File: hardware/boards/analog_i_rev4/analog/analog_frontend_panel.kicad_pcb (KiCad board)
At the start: 4 copper layers, 257 parts, among them IC1 INA826AIDR, IC10 INA826AIDR, IC1001 INA826AIDR, IC12 INA826AIDR, IC13 TLV333IDBVR, IC14 TLV333IDBVR, IC15 INA826AIDR, IC16 TLV333IDBVR, IC17 TLV333IDBVR, IC18 INA826AIDR, IC19 TLV333IDBVR, IC2 INA826AIDR, IC20 TLV333IDBVR, IC21 INA826AIDR, IC22 TLV333IDBVR, IC23 TLV333IDBVR, IC24 INA826AIDR, IC25 TLV333IDBVR, IC26 TLV333IDBVR, IC27 INA826AIDR, IC28 TLV333IDBVR, IC29 TLV333IDBVR, IC3 INA826AIDR, IC3001 INA826AIDR, IC3002 INA826AIDR, IC32001 BD42540FJ-CE2, IC33001 BD42540FJ-CE2, IC34001 BD42540FJ-CE2, IC35001 BD42540FJ-CE2, IC36001 BD42540FJ-CE2, IC4 INA826AIDR, IC5 INA826AIDR, IC6 INA826AIDR, IC7 INA826AIDR, IC8 INA826AIDR, J10 Screw_Terminal_01x03, J1001 Screw_Terminal_01x04, J11 Screw_Terminal_01x03, J12 AM-K-PCB, J13 AM-K-PCB, J14 AM-K-PCB, J15 AM-K-PCB, J16 Screw_Terminal_01x03, J17 Screw_Terminal_01x03, J18 Screw_Terminal_01x03, J19 Screw_Terminal_01x03, J20 Screw_Terminal_01x03, J22 Screw_Terminal_01x03, J3 Screw_Terminal_01x04, J3004 Screw_Terminal_01x04, J3005 Screw_Terminal_01x04, J4 Screw_Terminal_01x04, J5 Screw_Terminal_01x04, J8 Screw_Terminal_01x03, J9 Screw_Terminal_01x03, U1 NTJD4001NT1G, U1001 TLV3201AIDBVR, U1002 TLV3201AIDBVR, U1003 TLV3201AIDBVR, U1004 TLV3201AIDBVR, U1005 TLV3201AIDBVR, U2 NTJD4001NT1G, U3 NTJD4001NT1G, U4 NTJD4001NT1G, U5 NTJD4001NT1G, U6 NTJD4001NT1G

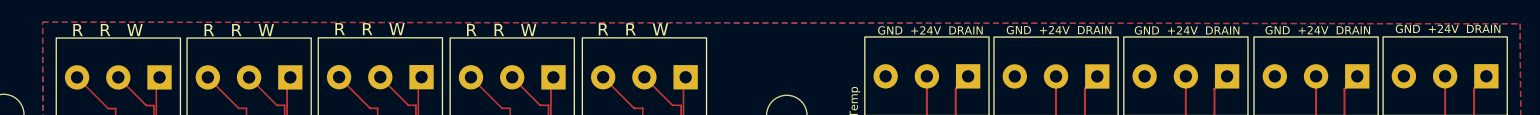
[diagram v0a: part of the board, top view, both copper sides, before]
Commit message: flip more silkscreen labels
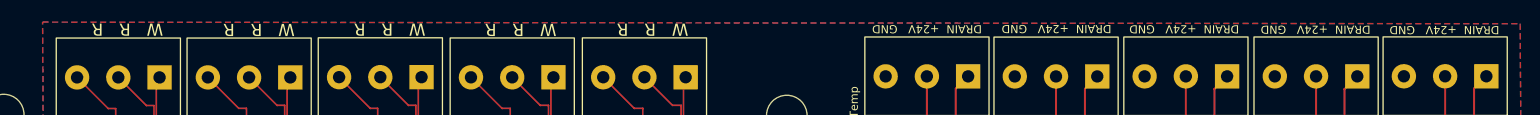
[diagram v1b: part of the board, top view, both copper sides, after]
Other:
- board text added: "DRAIN +24V GND"
- board text added: "W R R"
- board text removed: "GND +24V DRAIN"
- board text removed: "R R W"

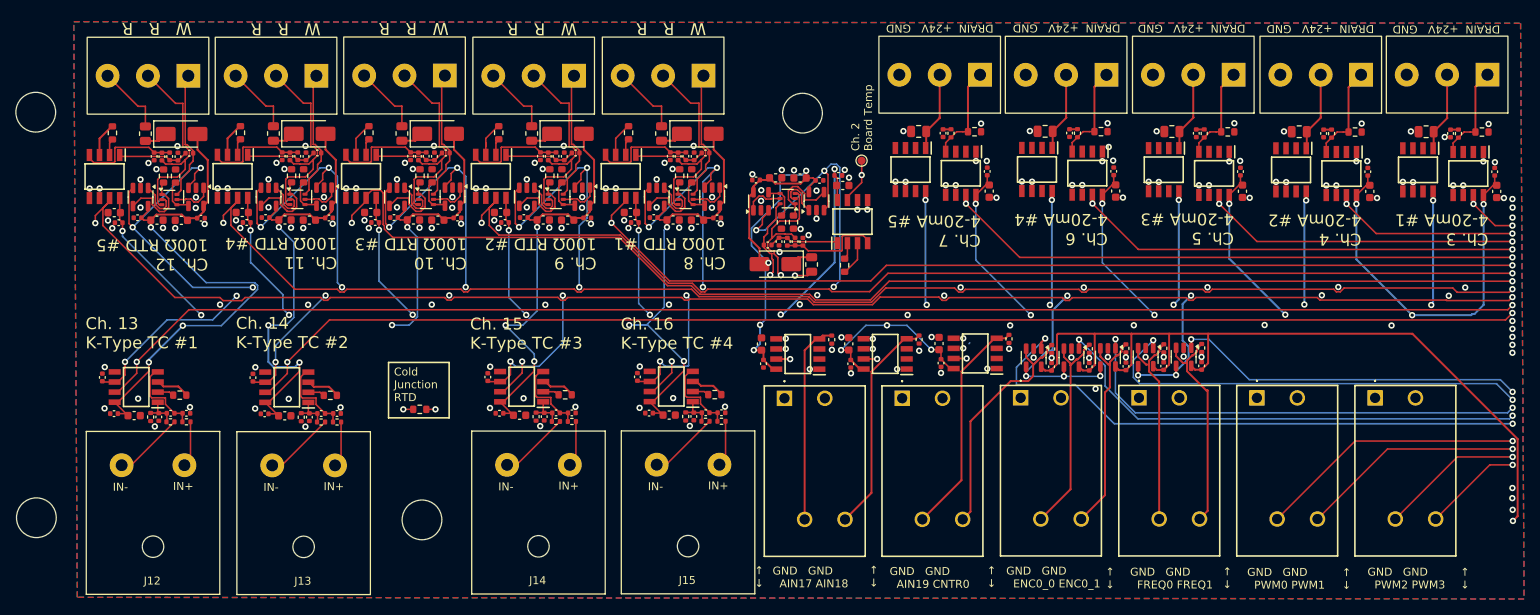
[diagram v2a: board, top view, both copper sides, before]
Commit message: Analog I Rev 4.0.2 (#17)
## 2025-02-22 Hardware - Analog I Rev 4.0.2

### Changed

* Replace input comparators with SN74LV Schmitt trigger logic buffers
* Adds about 0.5V hysteresis to resolve jitter & eliminates exposure of
1V024 ref to noise from digital signals
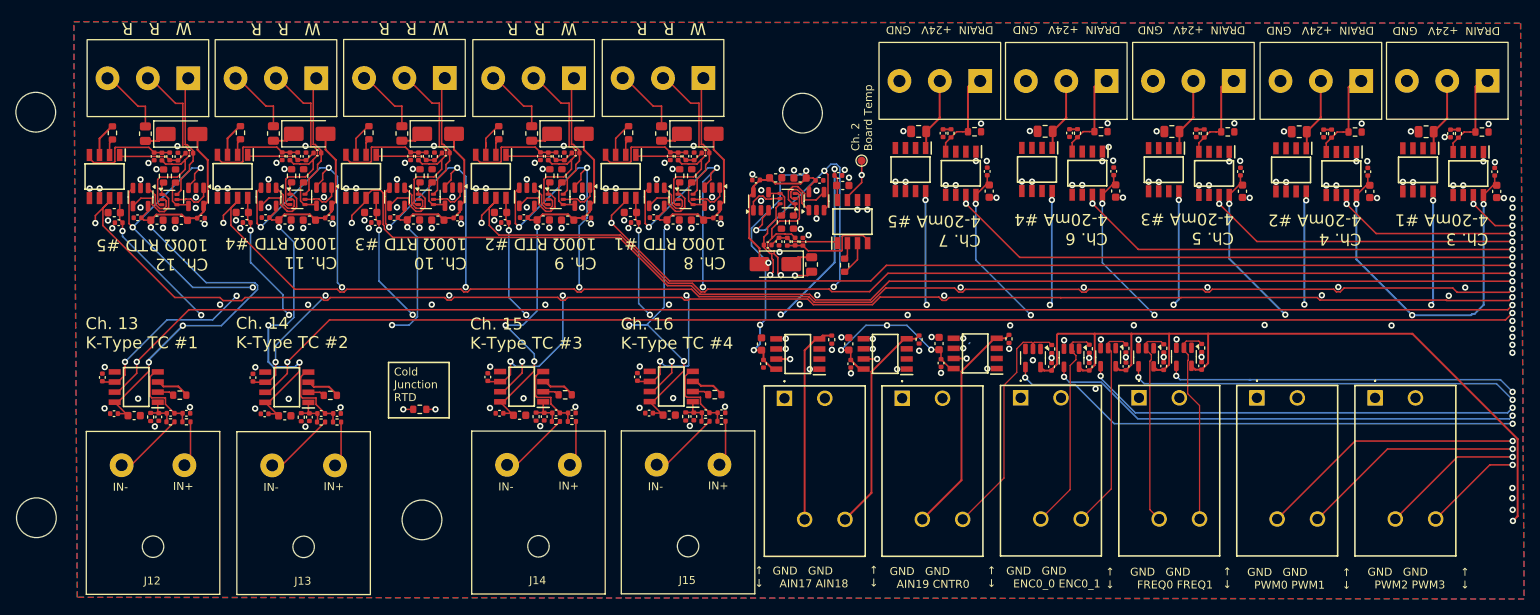
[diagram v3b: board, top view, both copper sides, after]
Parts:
- removed U1001, U1002, U1003, U1004, U1005: TLV3201AIDBVR, Package_TO_SOT_SMD:SOT-23-5
- added U10: 74LVC1G17, Package_TO_SOT_SMD:SOT-23-5, F.Cu at (224.0, 146.1)
- added U11: 74LVC1G17, Package_TO_SOT_SMD:SOT-23-5, F.Cu at (209.8, 146.2)
- added U7: 74LVC1G17, Package_TO_SOT_SMD:SOT-23-5, F.Cu at (219.2, 146.1)
- added U8: 74LVC1G17, Package_TO_SOT_SMD:SOT-23-5, F.Cu at (214.6, 146.2)
- added U9: 74LVC1G17, Package_TO_SOT_SMD:SOT-23-5, F.Cu at (228.8, 146.1)
- moved J16 0.78 mm to (267.0, 111.3)
- moved J17 0.78 mm to (251.1, 111.3)
- moved J18 0.78 mm to (235.0, 111.3)
- moved J19 0.78 mm to (219.0, 111.4)
- moved J22 0.78 mm to (203.1, 111.3)
- moved J10 0.31 mm to (135.8, 111.0)
- moved J9 0.31 mm to (152.0, 111.0)
- moved J11 0.31 mm to (119.6, 111.0)
- moved J20 0.31 mm to (103.5, 111.0)
- moved J8 0.31 mm to (168.3, 111.0)
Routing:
- net +1V024: track 290.6 -> 246.1 mm, vias 21 -> 14
- net /COUNTER0: track 73.3 -> 65.1 mm
- net /FREQ0: track 55.7 -> 49.7 mm
- net /ENCODER0_1: track 59.2 -> 55.4 mm
- net /FREQ1_PRE: track 27.2 -> 25.5 mm
- net /ENCODER0_0: track 61.5 -> 60.1 mm
- net /FREQ0_PRE: track 26.2 -> 25.4 mm
- net /ENCODER0_1_PRE: track 27.1 -> 26.3 mm
- net /AIN12: track 191.7 -> 191.1 mm
